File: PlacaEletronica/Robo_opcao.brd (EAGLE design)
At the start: 139.7 x 148 mm, 101 parts, among them IC1 7805DT, IC2 7805DT, J1 F-1X06-SIP-100-40, J2 S2B-PH-K-S(LF)(SN), J3 ZX62-B-5PA, Q1 SMD-TRANSISTORS-NPN-25V-500MW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, Q2 SMD-TRANSISTORS-NPN-25V-500MW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, Q4 SFH_3716, U1 ESP32-WROOM-32D, U2 AMS1117-3.3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

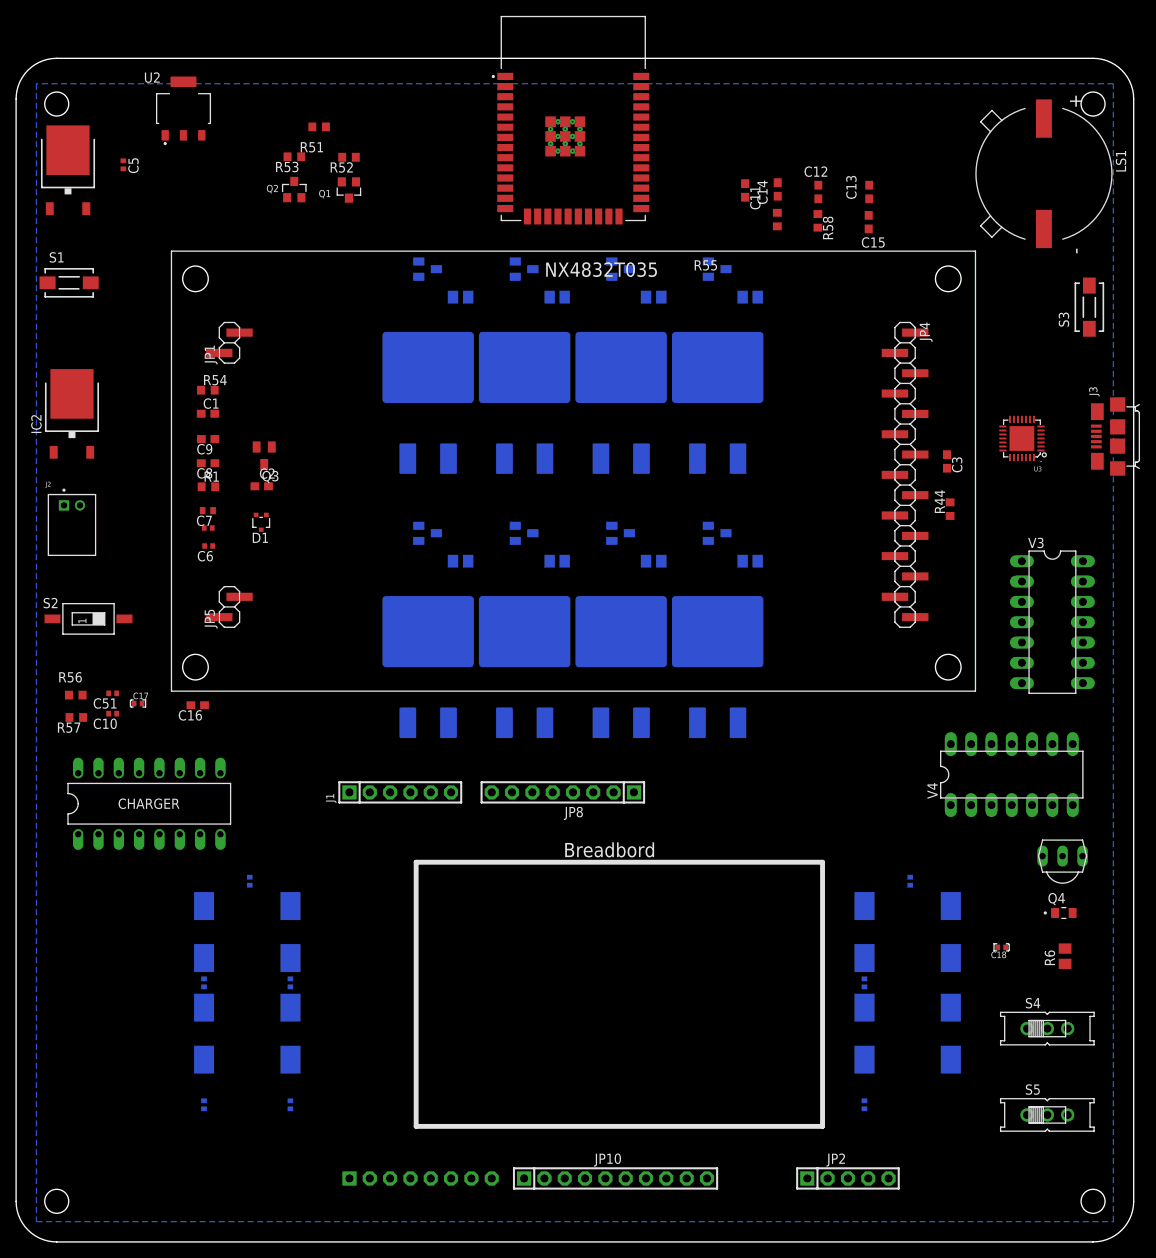
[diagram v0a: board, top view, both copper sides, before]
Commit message: PlacaPrincipal_AlteracoesResistoresCapacitoresPinhead
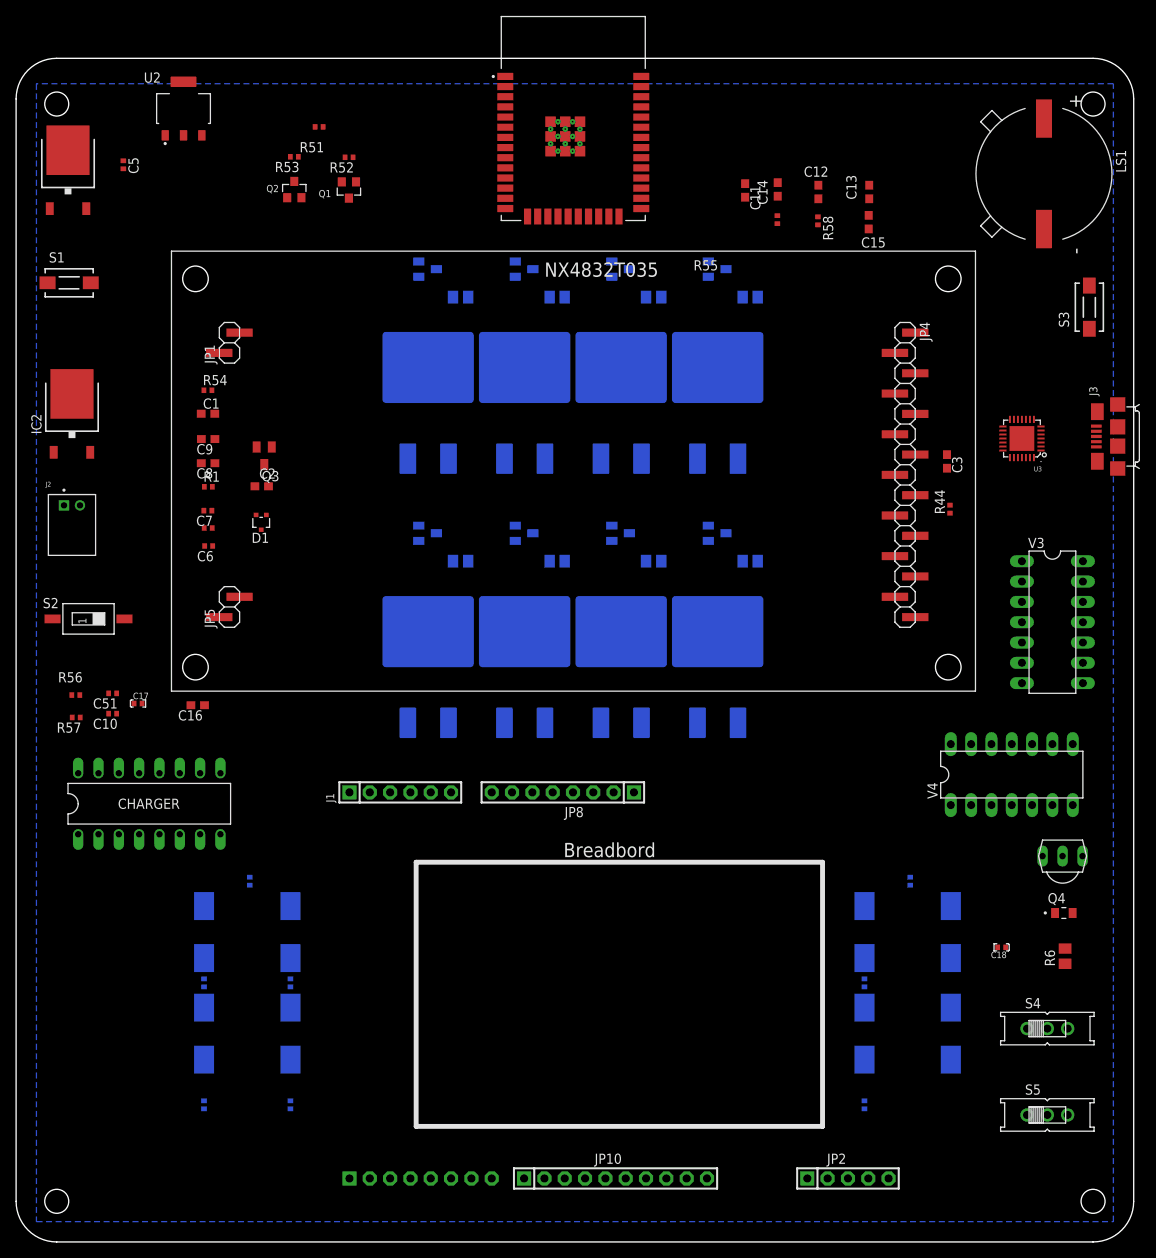
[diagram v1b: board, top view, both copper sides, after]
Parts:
- C7: device rcl:C0402 -> Perfect_0402:0402
- R1, R44, R51, R52, R54, R55, R56, R57, R58: device resistors:R0603_RESISTORS_LIB -> Perfect_0402:0402
- R53: device rcl:R0603 -> Perfect_0402:0402
